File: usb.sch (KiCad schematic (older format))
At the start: 33 parts, among them IC1 EP4CE10F17, P1 USB_A, U23 FT313HL-LQFP64-0.5, U25 TPS2024D, Y2 12MHz

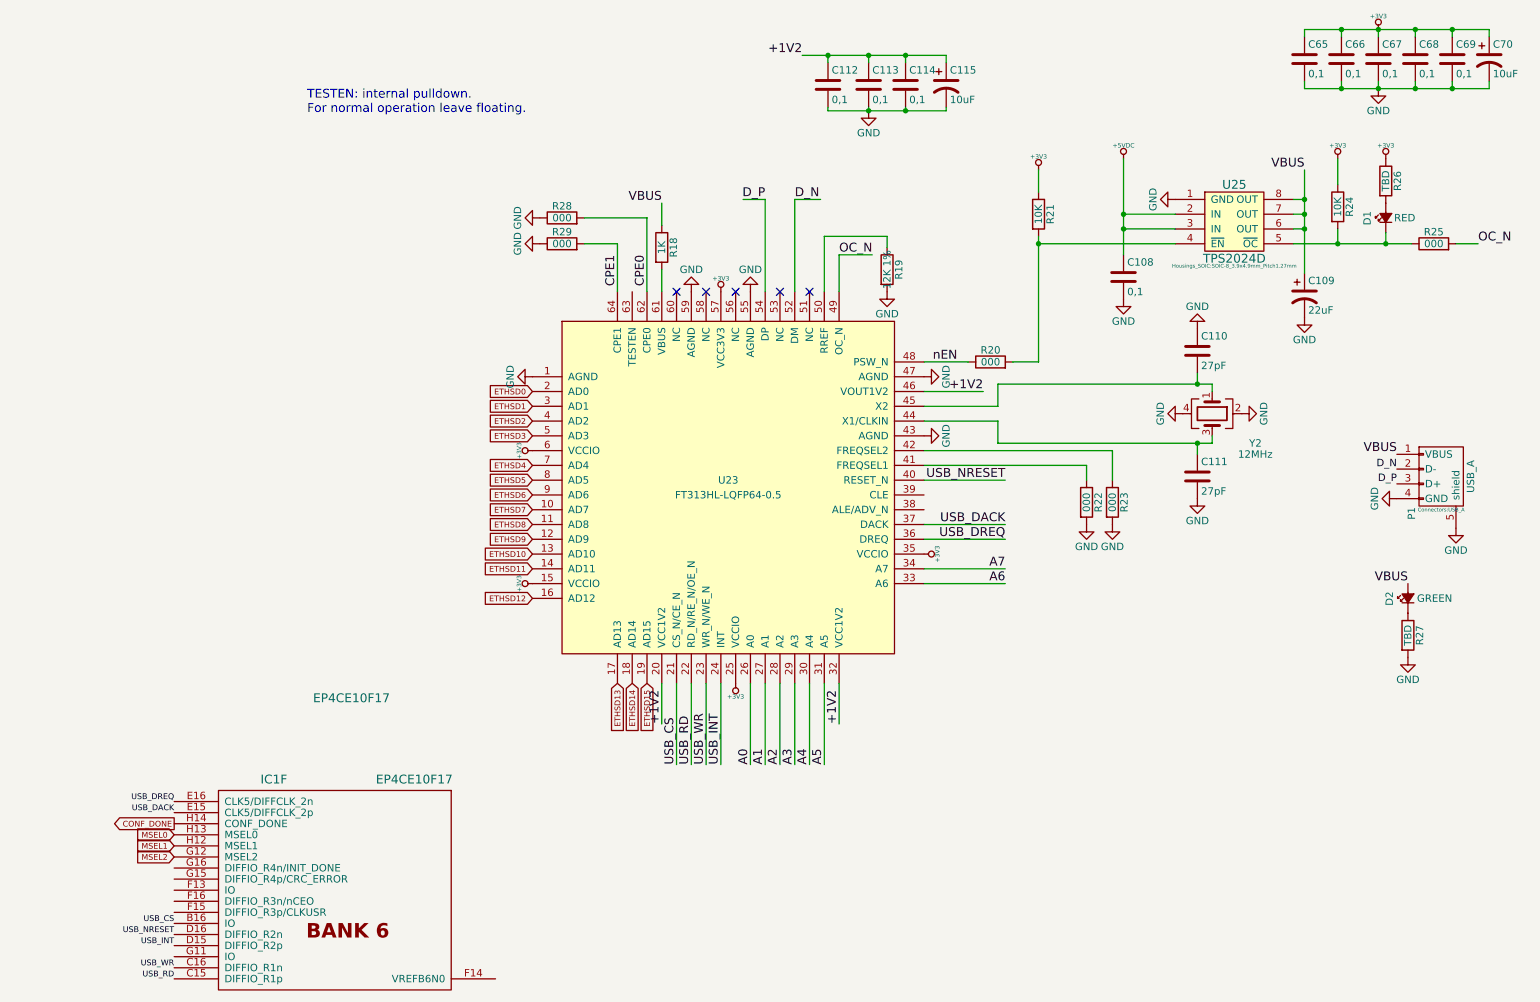
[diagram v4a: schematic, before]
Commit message: ALE and CLE routed
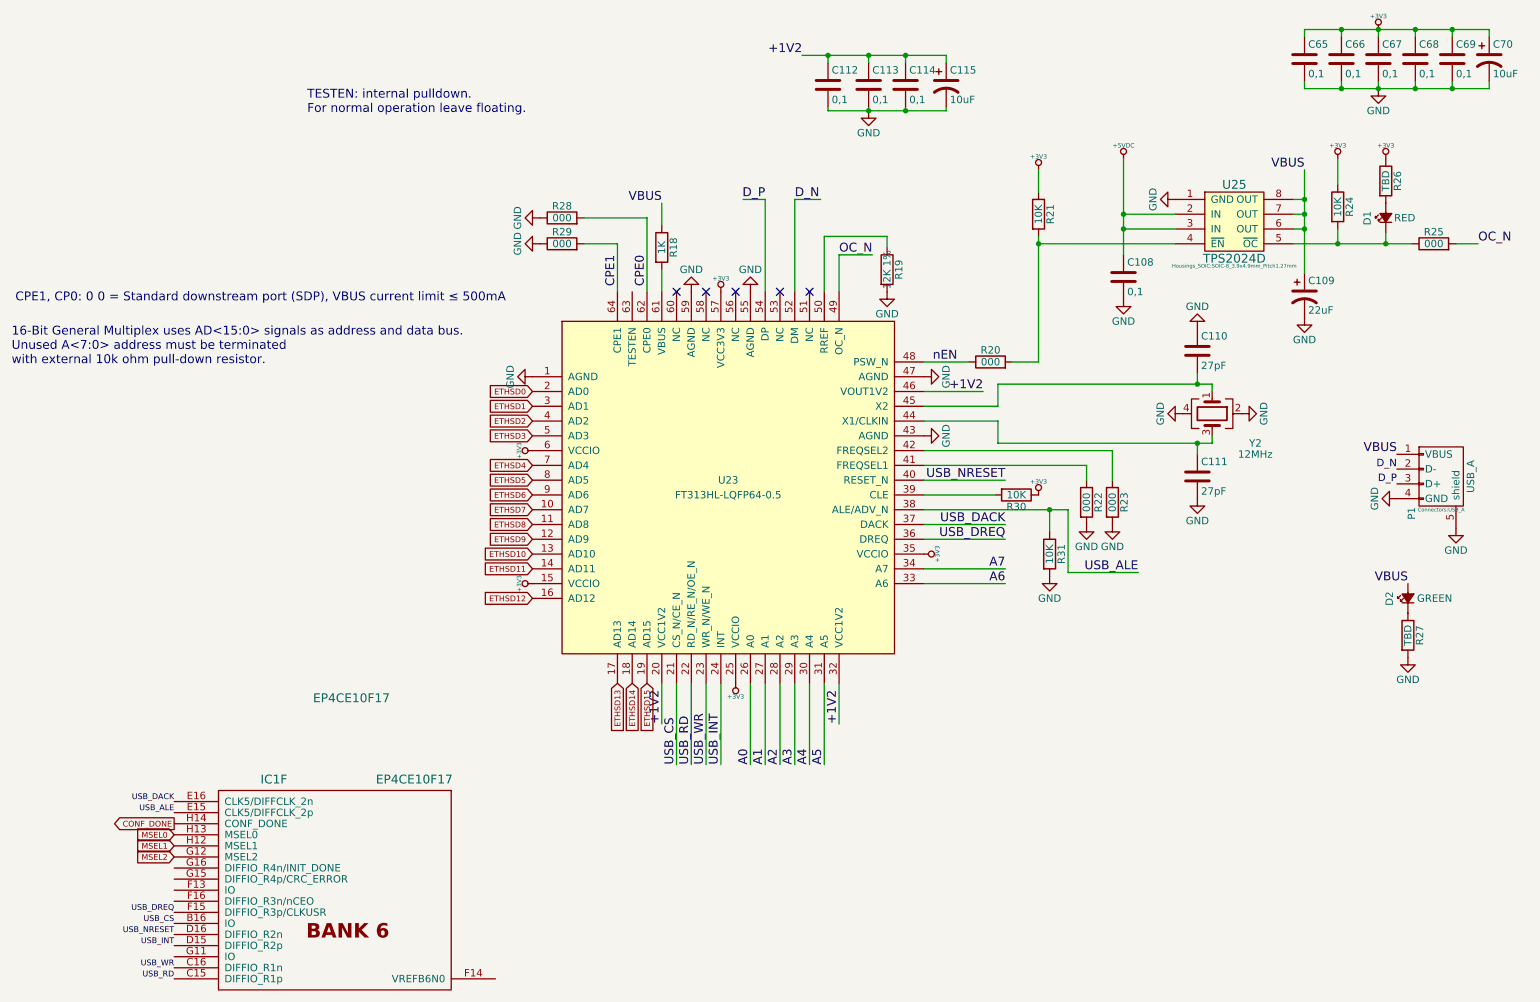
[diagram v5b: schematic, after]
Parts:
- added R30, R31: 10K, Resistors_SMD:R_0603, symbol R
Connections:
- net +3V3: now also R30.1
- net GND: now also R31.2
- net USB_DACK: now also IC1.E16 (CLK5/DIFFCLK_2n); no longer IC1.E15 (CLK5/DIFFCLK_2p)
- net USB_DREQ: now also IC1.F15 (DIFFIO_R3p/CLKUSR); no longer IC1.E16 (CLK5/DIFFCLK_2n)
- net USB_ALE: now reaches U23.38 (ALE/ADV_N)
- net USB_ALE: now also IC1.E15 (CLK5/DIFFCLK_2p), R31.1
- net at U23.39 (CLE): now also R30.2
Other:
- note added: "16-Bit General Multiplex uses AD<15:0> signals as address and data bus. \nUnused A<7:0> address must be terminated \nwith external 10k ohm pull-down resistor."
- note added: "CPE1, CP0: 0 0 = Standard downstream port (SDP), VBUS current limit ≤ 500mA"
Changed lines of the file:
@@
 NoConn ~ 5325 2450
 $Comp
-L GND #PWR141
+L GND #PWR0141
 U 1 1 587F93F7
 P 4350 3025
-F 0 "#PWR141" H 4350 2775 50  0001 C CNN
+F 0 "#PWR0141" H 4350 2775 50  0001 C CNN
 F 1 "GND" H 4350 2875 50  0000 C CNN
 F 2 "" H 4350 3025 50  0000 C CNN
@@
 $EndComp
 $Comp
-L GND #PWR153
+L GND #PWR0142
 U 1 1 587F942A
 P 7000 3425
-F 0 "#PWR153" H 7000 3175 50  0001 C CNN
+F 0 "#PWR0142" H 7000 3175 50  0001 C CNN
 F 1 "GND" H 7000 3275 50  0000 C CNN
 F 2 "" H 7000 3425 50  0000 C CNN
@@
 $EndComp
 $Comp
-L GND #PWR152
+L GND #PWR0143
 U 1 1 587F944F
 P 7000 3025
-F 0 "#PWR152" H 7000 2775 50  0001 C CNN
+F 0 "#PWR0143" H 7000 2775 50  0001 C CNN
 F 1 "GND" H 7000 2875 50  0000 C CNN
 F 2 "" H 7000 3025 50  0000 C CNN
@@
 $EndComp
 $Comp
-L GND #PWR149
+L GND #PWR0144
 U 1 1 587F9489
 P 5825 2450
-F 0 "#PWR149" H 5825 2200 50  0001 C CNN
+F 0 "#PWR0144" H 5825 2200 50  0001 C CNN
 F 1 "GND" H 5825 2300 50  0000 C CNN
 F 2 "" H 5825 2450 50  0000 C CNN
@@
 $EndComp
 $Comp
-L GND #PWR146
+L GND #PWR0145
 U 1 1 587F9497
 P 5425 2450
-F 0 "#PWR146" H 5425 2200 50  0001 C CNN
+F 0 "#PWR0145" H 5425 2200 50  0001 C CNN
 F 1 "GND" H 5425 2300 50  0000 C CNN
 F 2 "" H 5425 2450 50  0000 C CNN
@@
 $EndComp
 $Comp
-L +3V3 #PWR167
+L +3V3 #PWR0146
 U 1 1 587FA4A0
 P 10075 675
-F 0 "#PWR167" H 10175 725 20  0001 C CNN
+F 0 "#PWR0146" H 10175 725 20  0001 C CNN
 F 1 "+3V3" H 10075 765 30  0000 C CNN
 F 2 "" H 10075 675 60  0000 C CNN
@@
 $EndComp
 $Comp
-L GND #PWR168
+L GND #PWR0147
 U 1 1 587FA6CC
 P 10075 1075
-F 0 "#PWR168" H 10075 825 50  0001 C CNN
+F 0 "#PWR0147" H 10075 825 50  0001 C CNN
 F 1 "GND" H 10075 925 50  0000 C CNN
 F 2 "" H 10075 1075 50  0000 C CNN
@@
 $EndComp
 $Comp
-L +3V3 #PWR142
+L +3V3 #PWR0148
 U 1 1 587FB090
 P 4350 3525
-F 0 "#PWR142" H 4450 3575 20  0001 C CNN
+F 0 "#PWR0148" H 4450 3575 20  0001 C CNN
 F 1 "+3V3" H 4350 3615 30  0000 C CNN
 F 2 "" H 4350 3525 60  0000 C CNN
@@
 $EndComp
 $Comp
-L +3V3 #PWR148
+L +3V3 #PWR0149
 U 1 1 587FB177
 P 5725 5100
-F 0 "#PWR148" H 5825 5150 20  0001 C CNN
+F 0 "#PWR0149" H 5825 5150 20  0001 C CNN
 F 1 "+3V3" H 5725 5190 30  0000 C CNN
 F 2 "" H 5725 5100 60  0000 C CNN
@@
 $EndComp
 $Comp
-L +3V3 #PWR154
+L +3V3 #PWR0150
 U 1 1 587FB222
 P 7000 4225
-F 0 "#PWR154" H 7100 4275 20  0001 C CNN
+F 0 "#PWR0150" H 7100 4275 20  0001 C CNN
 F 1 "+3V3" H 7000 4315 30  0000 C CNN
 F 2 "" H 7000 4225 60  0000 C CNN
@@
 $EndComp
 $Comp
-L +3V3 #PWR143
+L +3V3 #PWR0151
 U 1 1 587FB43F
 P 4350 4425
-F 0 "#PWR143" H 4450 4475 20  0001 C CNN
+F 0 "#PWR0151" H 4450 4475 20  0001 C CNN
 F 1 "+3V3" H 4350 4515 30  0000 C CNN
 F 2 "" H 4350 4425 60  0000 C CNN
@@
 +1V2
 $Comp
-L +3V3 #PWR147
+L +3V3 #PWR0152
 U 1 1 587FFC16
 P 5625 2450
-F 0 "#PWR147" H 5725 2500 20  0001 C CNN
+F 0 "#PWR0152" H 5725 2500 20  0001 C CNN
 F 1 "+3V3" H 5625 2540 30  0000 C CNN
 F 2 "" H 5625 2450 60  0000 C CNN
@@
 Text Label 7550 4025 2    60   ~ 0
 USB_DACK
+Text Label 1925 6650 2    39   ~ 0
+USB_DREQ
 Text Label 1925 5900 2    39   ~ 0
-USB_DREQ
-Text Label 1925 5975 2    39   ~ 0
 USB_DACK
 Text Label 5925 1825 2    60   ~ 0
@@
 $EndComp
 $Comp
-L GND #PWR151
+L GND #PWR0153
 U 1 1 588FBF68
 P 6750 2450
-F 0 "#PWR151" H 6750 2200 50  0001 C CNN
+F 0 "#PWR0153" H 6750 2200 50  0001 C CNN
 F 1 "GND" H 6750 2300 50  0000 C CNN
 F 2 "" H 6750 2450 50  0000 C CNN
@@
 D_P
 $Comp
-L GND #PWR170
+L GND #PWR0154
 U 1 1 588FD418
 P 10200 3850
-F 0 "#PWR170" H 10200 3600 50  0001 C CNN
+F 0 "#PWR0154" H 10200 3600 50  0001 C CNN
 F 1 "GND" H 10200 3700 50  0000 C CNN
 F 2 "" H 10200 3850 50  0000 C CNN
@@
 $EndComp
 $Comp
-L GND #PWR172
+L GND #PWR0155
 U 1 1 588FDBE9
 P 10600 4050
-F 0 "#PWR172" H 10600 3800 50  0001 C CNN
+F 0 "#PWR0155" H 10600 3800 50  0001 C CNN
 F 1 "GND" H 10600 3900 50  0000 C CNN
 F 2 "" H 10600 4050 50  0000 C CNN
@@
 $EndComp
 $Comp
-L GND #PWR160
+L GND #PWR0156
 U 1 1 5890EDC6
 P 8700 1825
-F 0 "#PWR160" H 8700 1575 50  0001 C CNN
+F 0 "#PWR0156" H 8700 1575 50  0001 C CNN
 F 1 "GND" H 8700 1675 50  0000 C CNN
 F 2 "" H 8700 1825 50  0000 C CNN
@@
 $EndComp
 $Comp
-L GND #PWR159
+L GND #PWR0157
 U 1 1 5890F077
 P 8350 2500
-F 0 "#PWR159" H 8350 2250 50  0001 C CNN
+F 0 "#PWR0157" H 8350 2250 50  0001 C CNN
 F 1 "GND" H 8350 2350 50  0000 C CNN
 F 2 "" H 8350 2500 50  0000 C CNN
@@
 $EndComp
 $Comp
-L +3V3 #PWR155
+L +3V3 #PWR0158
 U 1 1 589100DF
 P 7775 1625
-F 0 "#PWR155" H 7875 1675 20  0001 C CNN
+F 0 "#PWR0158" H 7875 1675 20  0001 C CNN
 F 1 "+3V3" H 7775 1715 30  0000 C CNN
 F 2 "" H 7775 1625 60  0000 C CNN
@@
 $EndComp
 $Comp
-L +5VDC #PWR158
+L +5VDC #PWR0159
 U 1 1 58911317
 P 8350 1550
-F 0 "#PWR158" H 8450 1600 20  0001 C CNN
+F 0 "#PWR0159" H 8450 1600 20  0001 C CNN
 F 1 "+5VDC" H 8350 1640 30  0000 C CNN
 F 2 "" H 8350 1550 60  0000 C CNN
@@
 	8100 3625 7000 3625
 $Comp
-L GND #PWR156
+L GND #PWR0160
 U 1 1 58918521
 P 8100 4025
-F 0 "#PWR156" H 8100 3775 50  0001 C CNN
+F 0 "#PWR0160" H 8100 3775 50  0001 C CNN
 F 1 "GND" H 8100 3875 50  0000 C CNN
 F 2 "" H 8100 4025 50  0000 C CNN
@@
 $EndComp
 $Comp
-L GND #PWR157
+L GND #PWR0161
 U 1 1 58918565
 P 8275 4025
-F 0 "#PWR157" H 8275 3775 50  0001 C CNN
+F 0 "#PWR0161" H 8275 3775 50  0001 C CNN
 F 1 "GND" H 8275 3875 50  0000 C CNN
 F 2 "" H 8275 4025 50  0000 C CNN
@@
 $EndComp
 $Comp
-L +3V3 #PWR166
+L +3V3 #PWR0162
 U 1 1 58919A0E
 P 9800 1550
-F 0 "#PWR166" H 9900 1600 20  0001 C CNN
+F 0 "#PWR0162" H 9900 1600 20  0001 C CNN
 F 1 "+3V3" H 9800 1640 30  0000 C CNN
 F 2 "" H 9800 1550 60  0000 C CNN
@@
 $EndComp
 $Comp
-L GND #PWR165
+L GND #PWR0163
 U 1 1 5891AE93
 P 9575 2625
-F 0 "#PWR165" H 9575 2375 50  0001 C CNN
+F 0 "#PWR0163" H 9575 2375 50  0001 C CNN
 F 1 "GND" H 9575 2475 50  0000 C CNN
 F 2 "" H 9575 2625 50  0000 C CNN
@@
 $EndComp
 $Comp
-L GND #PWR161
+L GND #PWR0164
 U 1 1 5891C617
 P 8750 3275
-F 0 "#PWR161" H 8750 3025 50  0001 C CNN
+F 0 "#PWR0164" H 8750 3025 50  0001 C CNN
 F 1 "GND" H 8750 3125 50  0000 C CNN
 F 2 "" H 8750 3275 50  0000 C CNN
@@
 $EndComp
 $Comp
-L GND #PWR164
+L GND #PWR0165
 U 1 1 5891C65E
 P 9150 3275
-F 0 "#PWR164" H 9150 3025 50  0001 C CNN
+F 0 "#PWR0165" H 9150 3025 50  0001 C CNN
 F 1 "GND" H 9150 3125 50  0000 C CNN
 F 2 "" H 9150 3275 50  0000 C CNN
@@
 Connection ~ 8850 3075
 $Comp
-L GND #PWR163
+L GND #PWR0166
 U 1 1 5891DDB7
 P 8850 3850
-F 0 "#PWR163" H 8850 3600 50  0001 C CNN
+F 0 "#PWR0166" H 8850 3600 50  0001 C CNN
 F 1 "GND" H 8850 3700 50  0000 C CNN
 F 2 "" H 8850 3850 50  0000 C CNN
@@
 $EndComp
 $Comp
-L GND #PWR162
+L GND #PWR0167
 U 1 1 5891DE04
 P 8850 2700
-F 0 "#PWR162" H 8850 2450 50  0001 C CNN
+F 0 "#PWR0167" H 8850 2450 50  0001 C CNN
 F 1 "GND" H 8850 2550 50  0000 C CNN
 F 2 "" H 8850 2700 50  0000 C CNN
@@
 Connection ~ 6875 1225
 $Comp
-L GND #PWR150
+L GND #PWR0168
 U 1 1 58A7680E
 P 6625 1225
-F 0 "#PWR150" H 6625 975 50  0001 C CNN
+F 0 "#PWR0168" H 6625 975 50  0001 C CNN
 F 1 "GND" H 6625 1075 50  0000 C CNN
 F 2 "" H 6625 1225 50  0000 C CNN
@@
 $EndComp
 $Comp
-L GND #PWR171
+L GND #PWR0169
 U 1 1 5895CD67
 P 10275 4925
-F 0 "#PWR171" H 10275 4675 50  0001 C CNN
+F 0 "#PWR0169" H 10275 4675 50  0001 C CNN
 F 1 "GND" H 10275 4775 50  0000 C CNN
 F 2 "" H 10275 4925 50  0000 C CNN
@@
 $EndComp
 $Comp
-L +3V3 #PWR169
+L +3V3 #PWR0170
 U 1 1 5895DF10
 P 10125 1550
-F 0 "#PWR169" H 10225 1600 20  0001 C CNN
+F 0 "#PWR0170" H 10225 1600 20  0001 C CNN
 F 1 "+3V3" H 10125 1640 30  0000 C CNN
 F 2 "" H 10125 1550 60  0000 C CNN
@@
 $EndComp
 $Comp
-L GND #PWR144
+L GND #PWR0171
 U 1 1 5897A8C7
 P 4400 1950
-F 0 "#PWR144" H 4400 1700 50  0001 C CNN
+F 0 "#PWR0171" H 4400 1700 50  0001 C CNN
 F 1 "GND" H 4400 1800 50  0000 C CNN
 F 2 "" H 4400 1950 50  0000 C CNN
@@
 $EndComp
 $Comp
-L GND #PWR145
+L GND #PWR0172
 U 1 1 5897A935
 P 4400 2125
-F 0 "#PWR145" H 4400 1875 50  0001 C CNN
+F 0 "#PWR0172" H 4400 1875 50  0001 C CNN
 F 1 "GND" H 4400 1975 50  0000 C CNN
 F 2 "" H 4400 2125 50  0000 C CNN
@@
 Wire Wire Line
 	4925 2125 4700 2125
+Text Notes 850  2525 0    60   ~ 0
+CPE1, CP0: 0 0 = Standard downstream port (SDP), VBUS current limit ≤ 500mA
+Text Notes 825  2950 0    60   ~ 0
+16-Bit General Multiplex uses AD<15:0> signals as address and data bus. \nUnused A<7:0> address must be terminated \nwith external 10k ohm pull-down resistor.
+Wire Wire Line
+	7000 3825 7475 3825
+$Comp
+L R R30
+U 1 1 5898F563
+P 7625 3825
+F 0 "R30" V 7705 3825 50  0000 C CNN
+F 1 "10K" V 7625 3825 50  0000 C CNN
+F 2 "Resistors_SMD:R_0603" V 7555 3825 50  0001 C CNN
+F 3 "" H 7625 3825 50  0000 C CNN
+	1    7625 3825
+	0    1    1    0
+$EndComp
+$Comp
+L +3V3 #PWR0173
+U 1 1 5898F68C
+P 7775 3825
+F 0 "#PWR0173" H 7875 3875 20  0001 C CNN
+F 1 "+3V3" H 7775 3915 30  0000 C CNN
+F 2 "" H 7775 3825 60  0000 C CNN
+F 3 "" H 7775 3825 60  0000 C CNN
+	1    7775 3825
+	1    0    0    -1
+$EndComp
+$Comp
+L R R31
+U 1 1 5898FF52
+P 7850 4225
+F 0 "R31" V 7930 4225 50  0000 C CNN
+F 1 "10K" V 7850 4225 50  0000 C CNN
+F 2 "Resistors_SMD:R_0603" V 7780 4225 50  0001 C CNN
+F 3 "" H 7850 4225 50  0000 C CNN
+	1    7850 4225
+	1    0    0    -1
+$EndComp
+$Comp
+L GND #PWR0174
+U 1 1 589900C4
+P 7850 4375
+F 0 "#PWR0174" H 7850 4125 50  0001 C CNN
+F 1 "GND" H 7850 4225 50  0000 C CNN
+F 2 "" H 7850 4375 50  0000 C CNN
+F 3 "" H 7850 4375 50  0000 C CNN
+	1    7850 4375
+	1    0    0    -1
+$EndComp
+Wire Wire Line
+	7000 3925 7975 3925
+Wire Wire Line
+	7850 3925 7850 4075
+Connection ~ 7850 3925
+Wire Wire Line
+	7975 3925 7975 4350
+Wire Wire Line
+	7975 4350 8450 4350
+Text Label 8450 4350 2    60   ~ 0
+USB_ALE
+Text Label 1925 5975 2    39   ~ 0
+USB_ALE
 $EndSCHEMATC

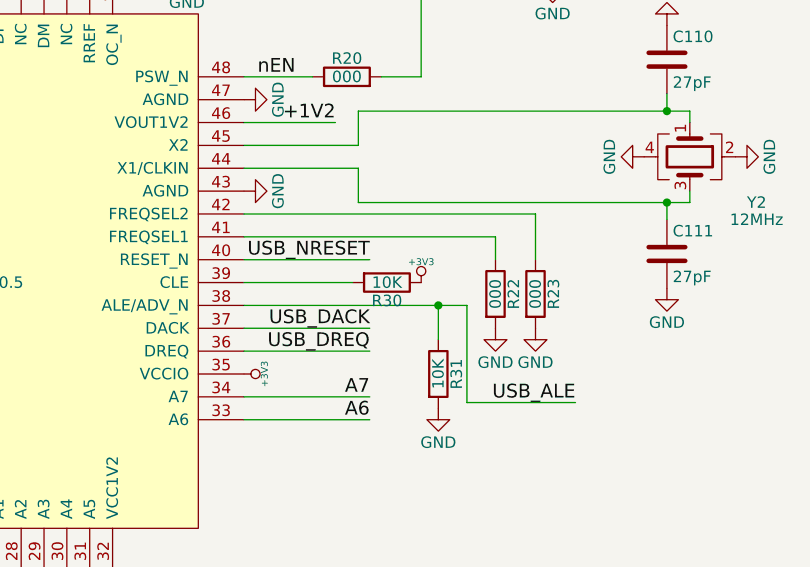
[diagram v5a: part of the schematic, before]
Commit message: FREQSEL eliminated
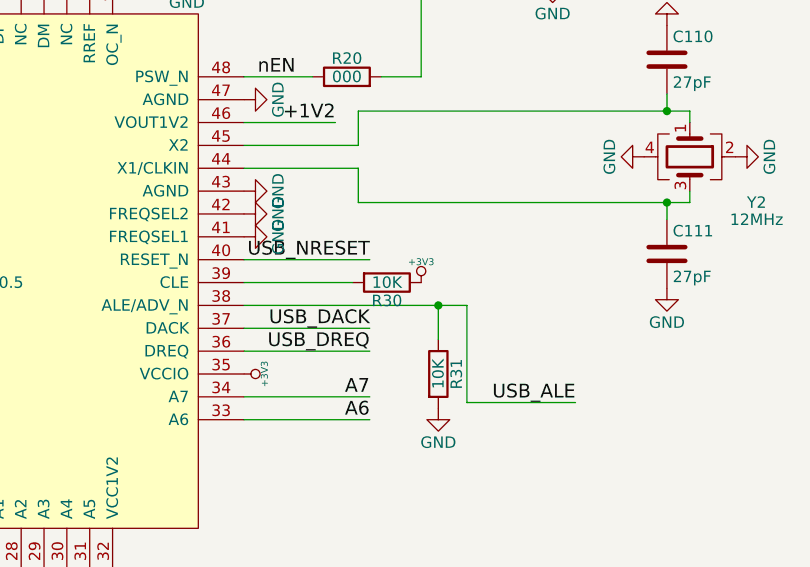
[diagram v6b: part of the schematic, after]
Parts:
- removed R22, R23: 000, Resistors_SMD:R_0603, symbol R
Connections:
- net GND: now also U23.41 (FREQSEL1), U23.42 (FREQSEL2)
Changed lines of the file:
@@
 	7500 3475 8950 3475
-$Comp
-L R R22
-U 1 1 58917A0F
-P 8100 3875
-F 0 "R22" V 8180 3875 50  0000 C CNN
-F 1 "000" V 8100 3875 50  0000 C CNN
-F 2 "Resistors_SMD:R_0603" V 8030 3875 50  0001 C CNN
-F 3 "" H 8100 3875 50  0000 C CNN
-	1    8100 3875
-	1    0    0    -1
-$EndComp
-$Comp
-L R R23
-U 1 1 58917B8F
-P 8275 3875
-F 0 "R23" V 8355 3875 50  0000 C CNN
-F 1 "000" V 8275 3875 50  0000 C CNN
-F 2 "Resistors_SMD:R_0603" V 8205 3875 50  0001 C CNN
-F 3 "" H 8275 3875 50  0000 C CNN
-	1    8275 3875
-	1    0    0    -1
-$EndComp
-Wire Wire Line
-	7000 3525 8275 3525
-Wire Wire Line
-	8275 3525 8275 3725
-Wire Wire Line
-	8100 3725 8100 3625
-Wire Wire Line
-	8100 3625 7000 3625
 $Comp
 L GND #PWR0160
 U 1 1 58918521
-P 8100 4025
-F 0 "#PWR0160" H 8100 3775 50  0001 C CNN
-F 1 "GND" H 8100 3875 50  0000 C CNN
-F 2 "" H 8100 4025 50  0000 C CNN
-F 3 "" H 8100 4025 50  0000 C CNN
-	1    8100 4025
-	1    0    0    -1
-$EndComp
-$Comp
-L GND #PWR0161
-U 1 1 58918565
-P 8275 4025
-F 0 "#PWR0161" H 8275 3775 50  0001 C CNN
-F 1 "GND" H 8275 3875 50  0000 C CNN
-F 2 "" H 8275 4025 50  0000 C CNN
-F 3 "" H 8275 4025 50  0000 C CNN
-	1    8275 4025
-	1    0    0    -1
+P 7000 3525
+F 0 "#PWR0160" H 7000 3275 50  0001 C CNN
+F 1 "GND" H 7000 3375 50  0000 C CNN
+F 2 "" H 7000 3525 50  0000 C CNN
+F 3 "" H 7000 3525 50  0000 C CNN
+	1    7000 3525
+	0    -1   -1   0
 $EndComp
 $Comp
@@
 Text Label 1925 5975 2    39   ~ 0
 USB_ALE
+$Comp
+L GND #PWR?
+U 1 1 5898F13F
+P 7000 3625
+F 0 "#PWR?" H 7000 3375 50  0001 C CNN
+F 1 "GND" H 7000 3475 50  0000 C CNN
+F 2 "" H 7000 3625 50  0000 C CNN
+F 3 "" H 7000 3625 50  0000 C CNN
+	1    7000 3625
+	0    -1   -1   0
+$EndComp
 $EndSCHEMATC
